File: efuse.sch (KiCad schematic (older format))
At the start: 31 parts, among them Q1701 BSS123, Q1702 BSS123, Q1703 BSS308, Q1704 BSS308, SW1301 SW_PUSH, U1701 MCP6H04, U1702 INA207, U1703 MEU1S1212ZC

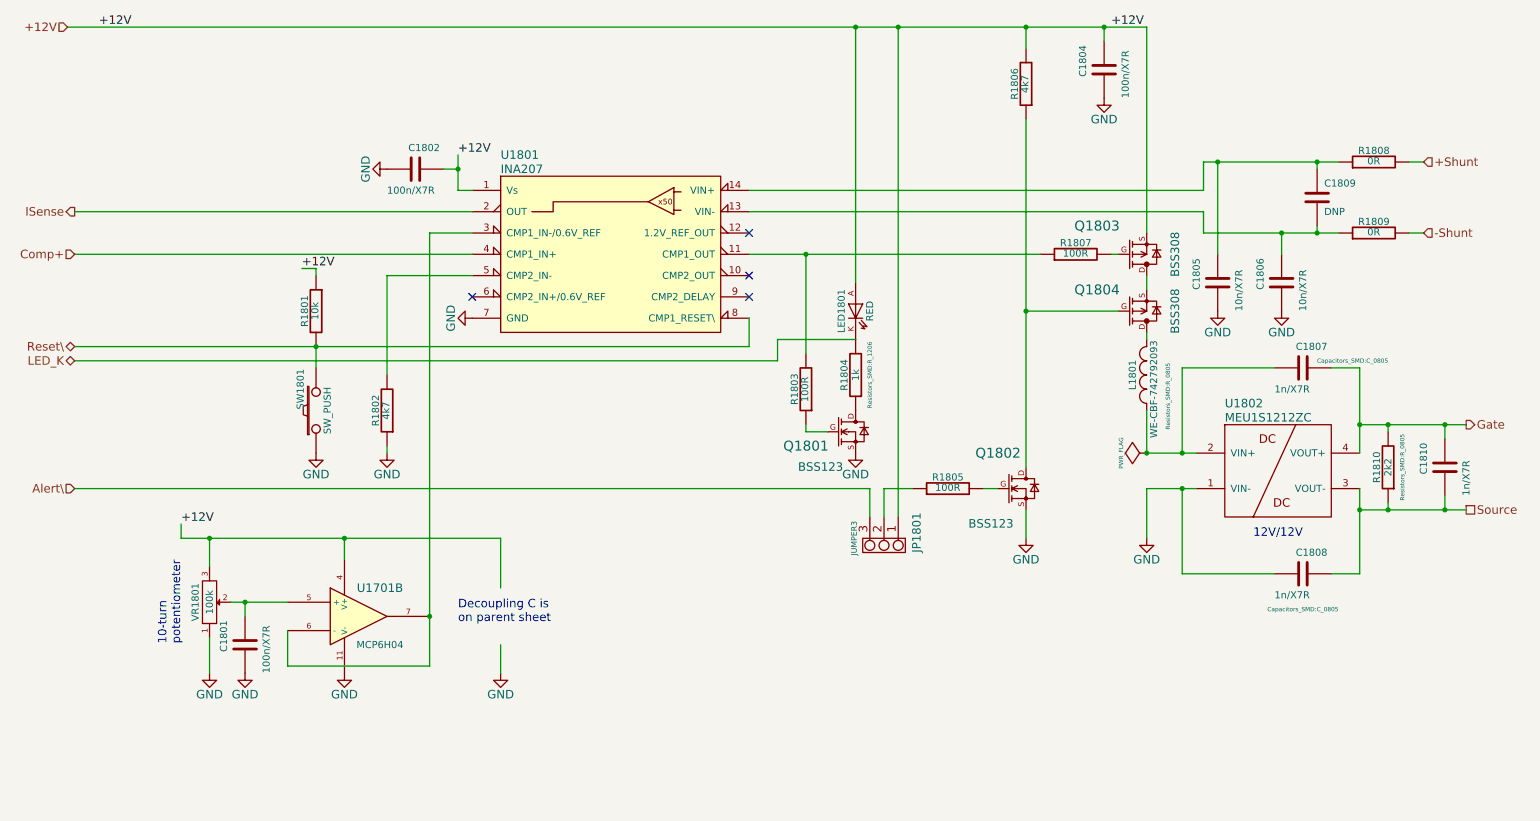
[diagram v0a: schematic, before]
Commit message: fixed missing Rs before Potis - fixed (removed) AD7294 Vpp connection
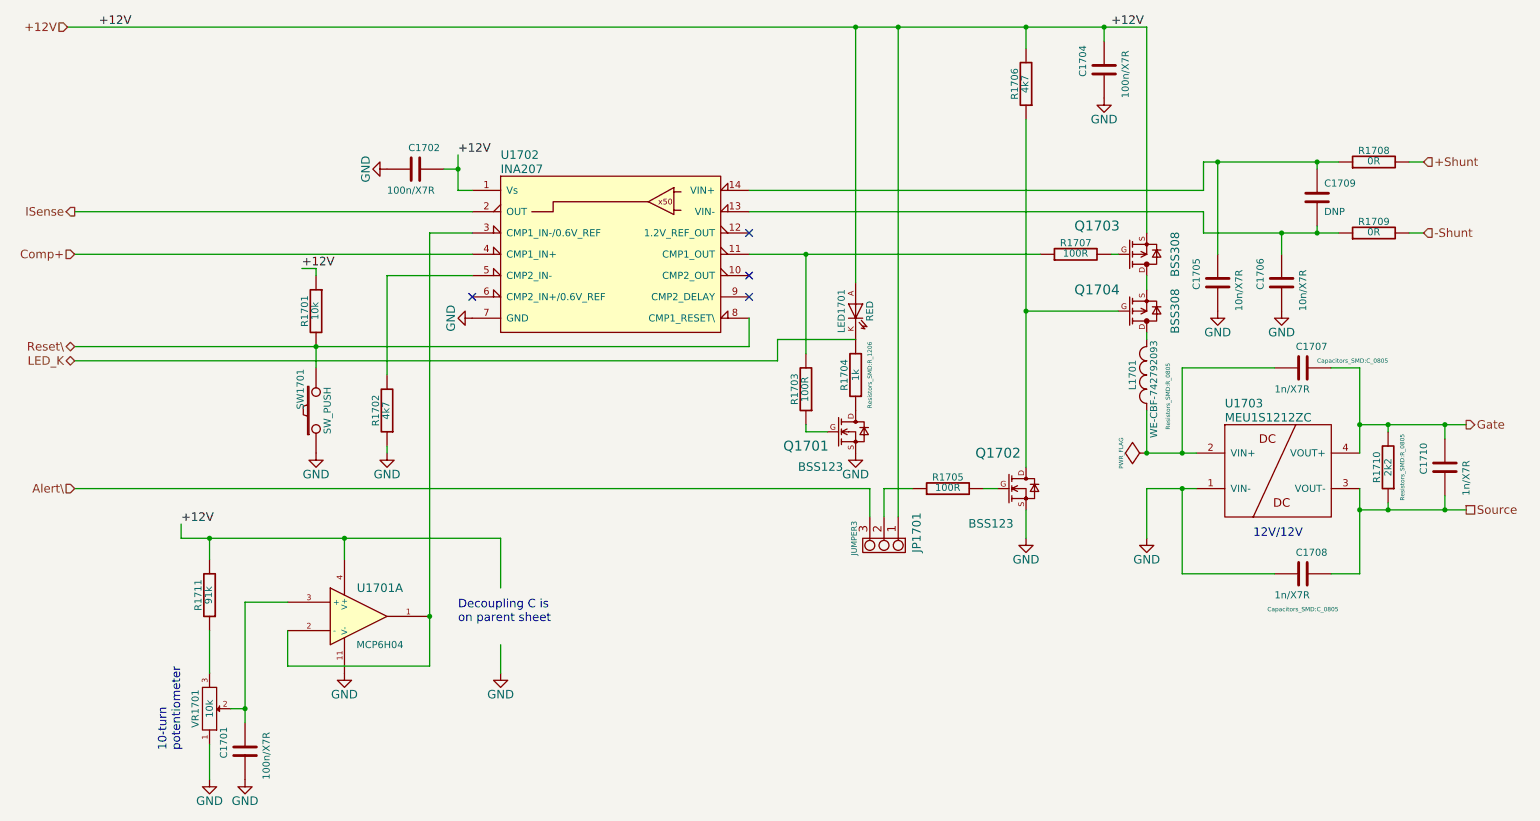
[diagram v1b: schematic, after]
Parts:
- added R1711: 91k, Resistors_SMD:R_0603, symbol R
- VR1701: value 100k -> 10k
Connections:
- net +12V: now also R1711.2; no longer VR1701.3
- net at C1301.1, VR1701.2: now also U1701.3 (+); no longer U1701.5 (+)
- new net: U1701.1, U1701.2 (-), U1702.3 (CMP1_IN-/0.6V_REF)
- new net: R1711.1, VR1701.3
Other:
- moved on the sheet: C1701, VR1701

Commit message: Rev B. Layout - Gerber/BOM need to be reexported
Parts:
- R1704: footprint Resistors_SMD:R_1206 -> Resistors_SMD:R_0805
- U1702: value INA207 -> INA206

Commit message: RevC
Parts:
- added R1712: 4k7, FT:0603, symbol R
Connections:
- net +12V: now also R1712.1
- net at R1703.2, R1707.1, U1702.11 (CMP1_OUT): now also R1712.2
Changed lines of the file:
@@
 LIBS:EtherDue_peripherals-cache
 LIBS:EtherDue_Power-cache
-LIBS:power
-LIBS:device
-LIBS:transistors
-LIBS:conn
-LIBS:linear
-LIBS:regul
-LIBS:74xx
-LIBS:cmos4000
-LIBS:adc-dac
-LIBS:memory
-LIBS:xilinx
-LIBS:microcontrollers
-LIBS:dsp
-LIBS:microchip
-LIBS:analog_switches
-LIBS:motorola
-LIBS:texas
-LIBS:intel
-LIBS:audio
-LIBS:interface
-LIBS:digital-audio
-LIBS:philips
-LIBS:display
-LIBS:cypress
-LIBS:siliconi
-LIBS:opto
-LIBS:atmel
-LIBS:contrib
-LIBS:valves
 LIBS:zeilhofer
 LIBS:w_transistor
@@
 $Descr A4 11693 8268
 encoding utf-8
-Sheet 17 20
+Sheet 18 20
 Title "High Frequency Power Amplifier Monitor on EtherDue"
 Date "2015-03-07"
@@
 Connection ~ 6450 950
 Wire Wire Line
-	6100 3250 6100 2550
+	6100 1650 6100 3250
 Connection ~ 6100 2550
 Wire Wire Line
@@
 Wire Wire Line
 	2150 5750 2050 5750
+$Comp
+L R R1712
+U 1 1 5A0EEDEE
+P 6100 1400
+AR Path="/54EFA122/5A0EEDEE" Ref="R1712"  Part="1"
+AR Path="/54FB135E/5A0EEDEE" Ref="R1812"  Part="1"
+AR Path="/54FB5450/5A0EEDEE" Ref="R1912"  Part="1"
+F 0 "R1712" V 6180 1400 50  0000 C CNN
+F 1 "4k7" V 6107 1401 50  0000 C CNN
+F 2 "FT:0603" V 6030 1400 30  0000 C CNN
+F 3 "" H 6100 1400 30  0000 C CNN
+	1    6100 1400
+	1    0    0    -1
+$EndComp
+Wire Wire Line
+	6100 1150 6100 950
+Connection ~ 6100 950
 $EndSCHEMATC
